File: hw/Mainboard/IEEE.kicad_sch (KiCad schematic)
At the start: 26 parts, among them J10 IEEE_HEADER, J11 IEEE, U14 74LS245, U15 SN74LS07, U16 SN74LS07, U17 74LS245, U18 SN74LS07

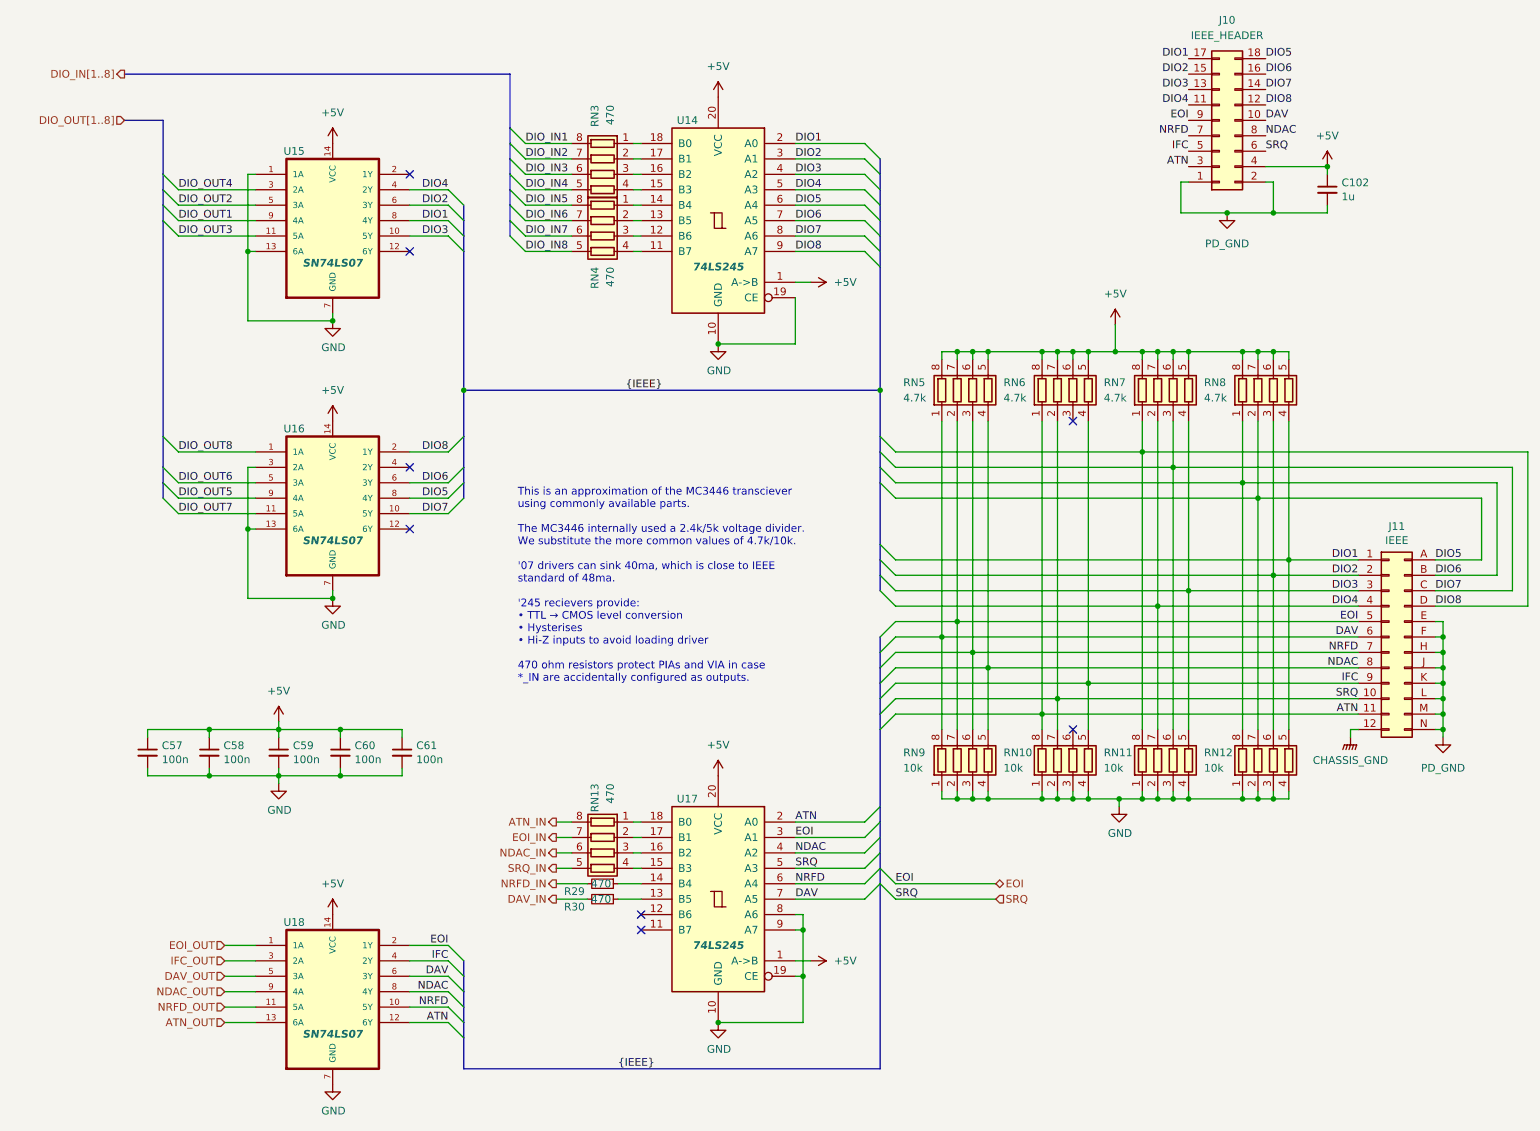
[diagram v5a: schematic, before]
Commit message: hw: renumber J* refs to match PET connectors
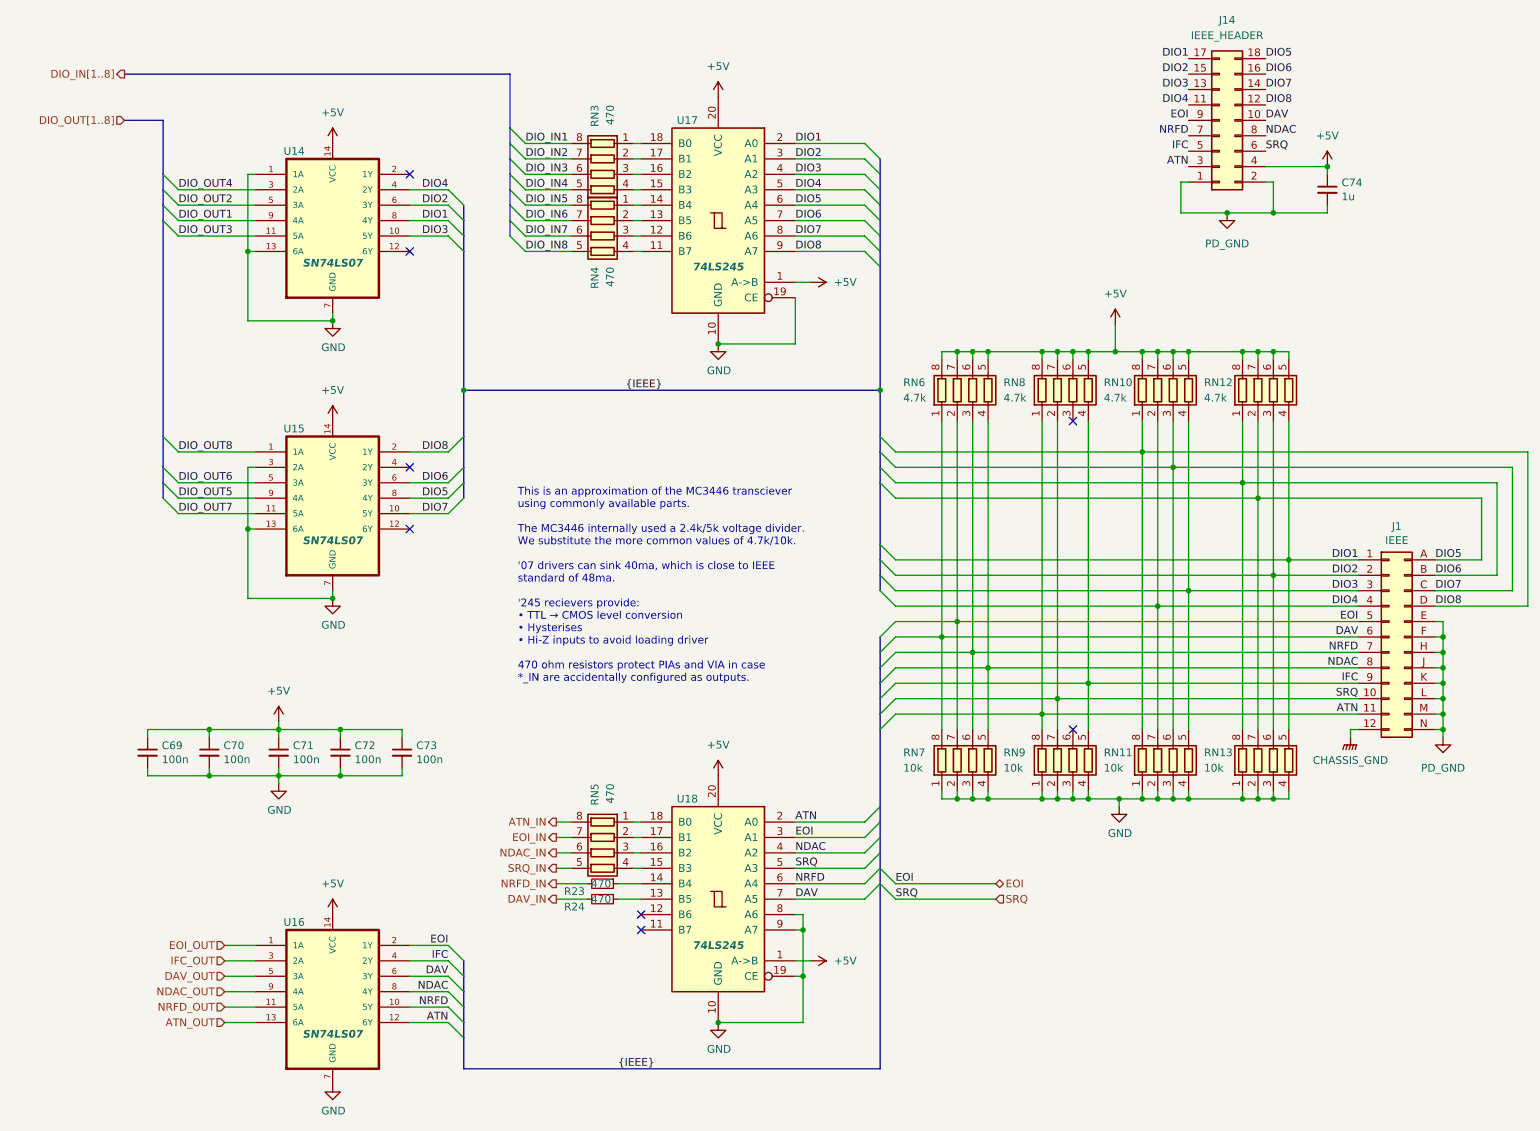
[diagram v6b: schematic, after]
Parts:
- renumbered C57 to C69, C58 to C70, C59 to C71, C60 to C72, C61 to C73, C102 to C74, J11 to J1, J10 to J14, R29 to R23, R30 to R24, RN7 to RN10, RN8 to RN12, RN12 to RN13, RN13 to RN5, RN5 to RN6, RN9 to RN7, RN6 to RN8, RN10 to RN9, U15 to U14, U16 to U15, U18 to U16, U14 to U17, U17 to U18

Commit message: hw: renumber rn.  tidy fpga schematics
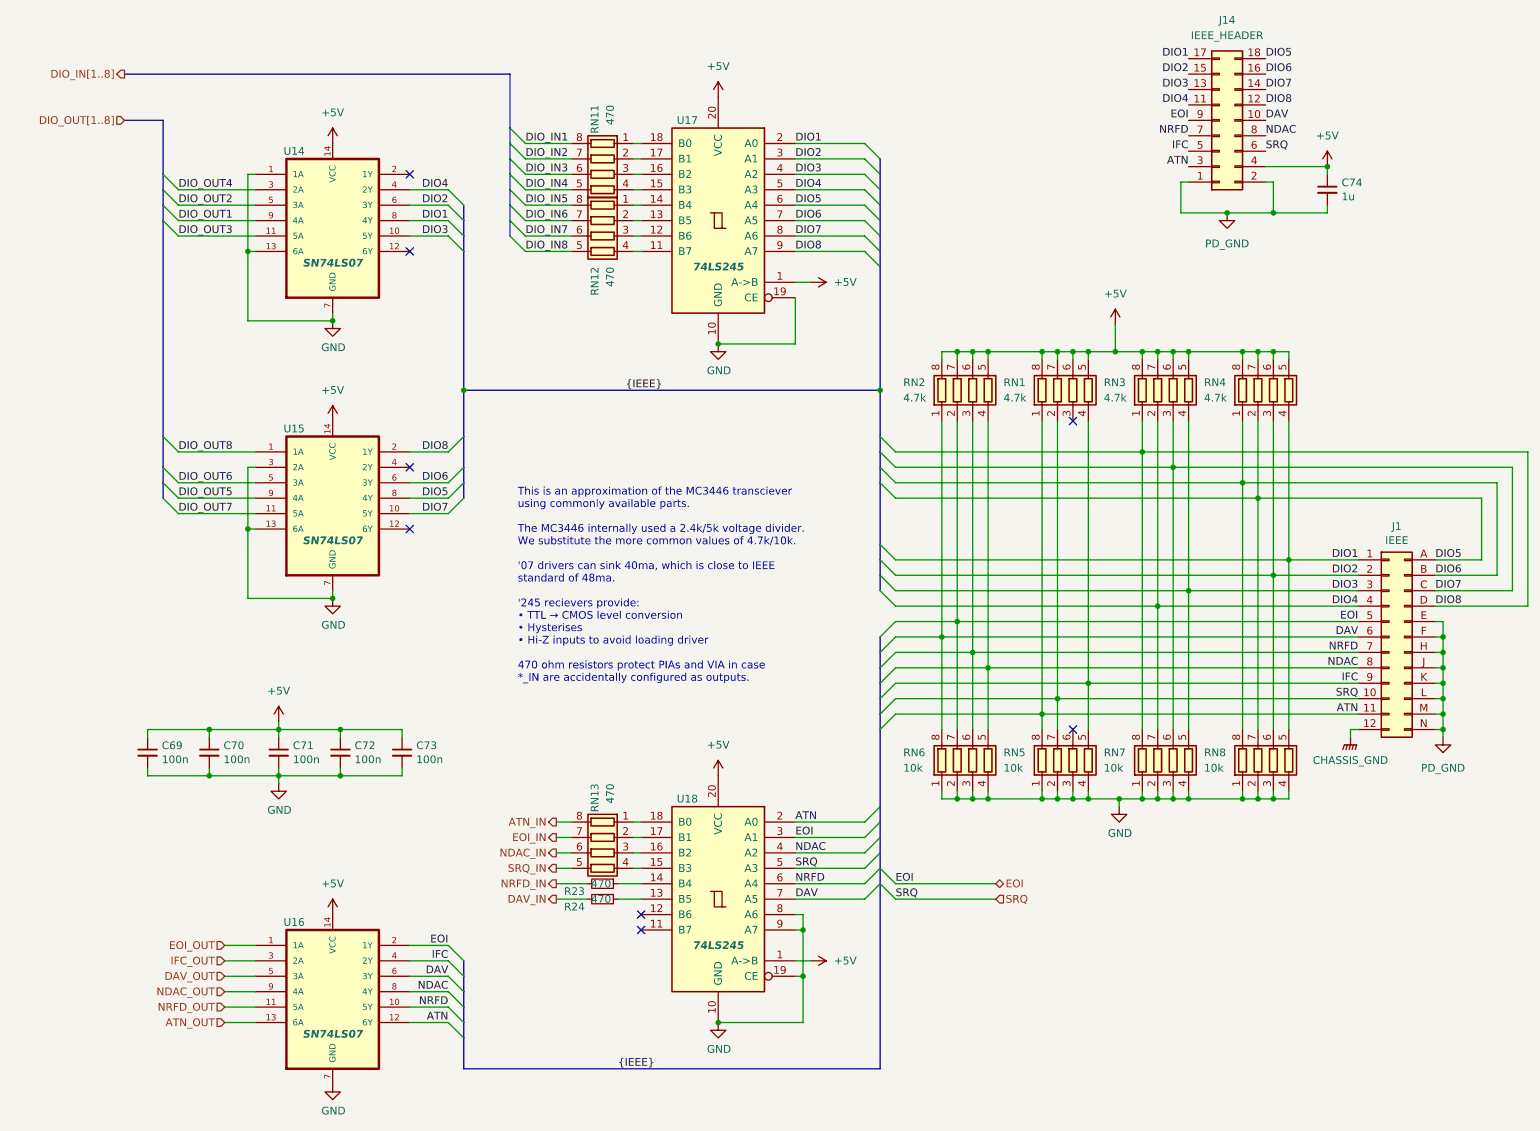
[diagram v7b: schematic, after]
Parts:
- renumbered RN8 to RN1, RN3 to RN11, RN4 to RN12, RN5 to RN13, RN6 to RN2, RN10 to RN3, RN12 to RN4, RN9 to RN5, RN7 to RN6, RN11 to RN7, RN13 to RN8
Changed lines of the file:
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@@
   (symbol (lib_id "Device:R_Pack04") (at 109.22 53.34 90) (mirror x) (unit 1)
     (in_bom yes) (on_board yes)
-    (property "Reference" "RN4" (id 0) (at 107.95 58.42 0)
+    (property "Reference" "RN12" (id 0) (at 107.95 58.42 0)
       (effects (font (size 1.27 1.27)) (justify left))
     )
@@
   (symbol (lib_id "Device:R_Pack04") (at 170.18 139.7 0) (unit 1)
     (in_bom yes) (on_board yes)
-    (property "Reference" "RN7" (id 0) (at 158.75 138.43 0)
+    (property "Reference" "RN6" (id 0) (at 158.75 138.43 0)
       (effects (font (size 1.27 1.27)) (justify left))
     )
@@
   (symbol (lib_id "Device:R_Pack04") (at 219.71 139.7 0) (unit 1)
     (in_bom yes) (on_board yes)
-    (property "Reference" "RN13" (id 0) (at 208.28 138.43 0)
+    (property "Reference" "RN8" (id 0) (at 208.28 138.43 0)
       (effects (font (size 1.27 1.27)) (justify left))
     )
@@
   (symbol (lib_id "Device:R_Pack04") (at 219.71 78.74 0) (unit 1)
     (in_bom yes) (on_board yes)
-    (property "Reference" "RN12" (id 0) (at 208.28 77.47 0)
+    (property "Reference" "RN4" (id 0) (at 208.28 77.47 0)
       (effects (font (size 1.27 1.27)) (justify left))
     )
@@
   (symbol (lib_id "Device:R_Pack04") (at 109.22 43.18 90) (mirror x) (unit 1)
     (in_bom yes) (on_board yes)
-    (property "Reference" "RN3" (id 0) (at 107.95 31.75 0)
+    (property "Reference" "RN11" (id 0) (at 107.95 31.75 0)
       (effects (font (size 1.27 1.27)) (justify left))
     )
@@
   (symbol (lib_id "Device:R_Pack04") (at 186.69 139.7 0) (unit 1)
     (in_bom yes) (on_board yes)
-    (property "Reference" "RN9" (id 0) (at 175.26 138.43 0)
+    (property "Reference" "RN5" (id 0) (at 175.26 138.43 0)
       (effects (font (size 1.27 1.27)) (justify left))
     )
@@
   (symbol (lib_id "Device:R_Pack04") (at 109.22 154.94 90) (mirror x) (unit 1)
     (in_bom yes) (on_board yes)
-    (property "Reference" "RN5" (id 0) (at 107.95 143.51 0)
+    (property "Reference" "RN13" (id 0) (at 107.95 143.51 0)
       (effects (font (size 1.27 1.27)) (justify left))
     )
@@
   (symbol (lib_id "Device:R_Pack04") (at 186.69 78.74 0) (unit 1)
     (in_bom yes) (on_board yes)
-    (property "Reference" "RN8" (id 0) (at 175.26 77.47 0)
+    (property "Reference" "RN1" (id 0) (at 175.26 77.47 0)
       (effects (font (size 1.27 1.27)) (justify left))
     )
@@
   (symbol (lib_id "Device:R_Pack04") (at 170.18 78.74 0) (unit 1)
     (in_bom yes) (on_board yes)
-    (property "Reference" "RN6" (id 0) (at 158.75 77.47 0)
+    (property "Reference" "RN2" (id 0) (at 158.75 77.47 0)
       (effects (font (size 1.27 1.27)) (justify left))
     )
@@
   (symbol (lib_id "Device:R_Pack04") (at 203.2 139.7 0) (unit 1)
     (in_bom yes) (on_board yes)
-    (property "Reference" "RN11" (id 0) (at 191.77 138.43 0)
+    (property "Reference" "RN7" (id 0) (at 191.77 138.43 0)
       (effects (font (size 1.27 1.27)) (justify left))
     )
@@
   (symbol (lib_id "Device:R_Pack04") (at 203.2 78.74 0) (unit 1)
     (in_bom yes) (on_board yes)
-    (property "Reference" "RN10" (id 0) (at 191.77 77.47 0)
-      (effects (font (size 1.27 1.27)) (justify left))
-    )
+    (property "Reference" "RN3" (id 0) (at 191.77 77.47 0)
+      (effects (font (size 1.27 1.27)) (justify left))
+    )
